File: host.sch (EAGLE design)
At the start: 109 parts, among them IC1 74LVC1T45GS,132, IC10 74LVC1T45GS,132, IC11 74LVC1T45GS,132, IC2 NCP187AMT120TAG, IC3 LD39200PU33R, IC4 74LVC1T45GS,132, IC5 74LVC1T45GS,132, IC6 74LVC1T45GS,132, IC7 74ALVC164245DGG:11, IC8 74ALVC164245DGG:11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

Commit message: Running through the checklist
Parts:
- added DONE: GREEN-0603, Seeed-LED:SMD-LED-CLEAR-GREEN(0603)
- added IC12: MMBT3904T, host:MMBT3904T
- added R29: 10K, rcl:R-EU_R0201
- added R30: 100K, rcl:R-EU_R0201
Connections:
- new net N$5: IC12.B, R30.2
- new net N$6: DONE.-, IC12.C
- new net N$7: DONE.+, R29.2
- net !STATUS!: now also U$1-RIGHT.GPIOL_71_!STATUS!@136
- net +3V3: now also R29.1
- net CDONE: now also R30.1
- net GND: now also IC12.E, IC7.1A7, IC7.1B7
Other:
- note added: "Checklist: [x] All power-pin checklist items [ ] Got as far as doing CDONE on configuration items"
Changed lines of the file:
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@@
 <setting verticaltext="up"/>
 </settings>
-<grid distance="0.1" unitdist="inch" unit="inch" style="lines" multiple="1" display="yes" altdistance="0.01" altunitdist="inch" altunit="inch"/>
+<grid distance="0.1" unitdist="inch" unit="inch" style="lines" multiple="1" display="no" altdistance="0.01" altunitdist="inch" altunit="inch"/>
 <layers>
 <layer number="1" name="Top" color="4" fill="1" visible="no" active="no"/>
@@
 <part name="SUPPLY28" library="supply2" deviceset="GND" device=""/>
 <part name="SUPPLY29" library="supply2" deviceset="GND" device=""/>
+<part name="DONE" library="Seeed-LED" deviceset="SMD-LED-CLEAR-GREEN(0603)" device="" value="GREEN-0603">
+<attribute name="USE" value="SML-E12M8WT86"/>
+</part>
+<part name="R29" library="rcl" library_urn="urn:adsk.eagle:library:334" deviceset="R-EU_" device="R0201" package3d_urn="urn:adsk.eagle:package:26117/2" value="10K">
+<attribute name="USE" value="WR02X221 JAL"/>
+</part>
+<part name="R30" library="rcl" library_urn="urn:adsk.eagle:library:334" deviceset="R-EU_" device="R0201" package3d_urn="urn:adsk.eagle:package:26117/2" value="100K">
+<attribute name="USE" value="PFR03S-104-JNH"/>
+</part>
+<part name="IC12" library="host" deviceset="MMBT3904T" device="">
+<attribute name="USE" value="MMBT3904T-7-F"/>
+</part>
+<part name="SUPPLY30" library="supply2" deviceset="GND" device=""/>
+<part name="+3V32" library="sjg-supply1" deviceset="+3V3" device=""/>
 </parts>
 <sheets>
 <sheet>
 <plain>
+<text x="12.7" y="243.84" size="1.778" layer="94">Checklist:
+[x]        All power-pin checklist items
+[ ]         Got as far as doing CDONE on configuration items</text>
 </plain>
 <instances>
@@
 <attribute name="VALUE" x="159.385" y="-125.095" size="1.778" layer="96"/>
 </instance>
+<instance part="DONE" gate="G$1" x="452.12" y="-20.32" smashed="yes" rot="R270">
+<attribute name="NAME" x="453.39" y="-12.7" size="1.27" layer="95" ratio="10" rot="R270"/>
+<attribute name="VALUE" x="447.04" y="-15.24" size="1.27" layer="96" ratio="10" rot="R270"/>
+<attribute name="USE" x="452.12" y="-20.32" size="1.778" layer="96" rot="R270" display="off"/>
+</instance>
+<instance part="R29" gate="G$1" x="452.12" y="-2.54" smashed="yes" rot="R270">
+<attribute name="NAME" x="453.6186" y="1.27" size="1.778" layer="95" rot="R270"/>
+<attribute name="VALUE" x="448.818" y="1.27" size="1.778" layer="96" rot="R270"/>
+<attribute name="USE" x="452.12" y="-2.54" size="1.778" layer="96" rot="R270" display="off"/>
+</instance>
+<instance part="R30" gate="G$1" x="421.64" y="-45.72" smashed="yes">
+<attribute name="NAME" x="417.83" y="-44.2214" size="1.778" layer="95"/>
+<attribute name="VALUE" x="417.83" y="-49.022" size="1.778" layer="96"/>
+<attribute name="USE" x="421.64" y="-45.72" size="1.778" layer="96" display="off"/>
+</instance>
+<instance part="IC12" gate="G$1" x="447.04" y="-45.72" smashed="yes">
+<attribute name="NAME" x="454.66" y="-38.1" size="1.778" layer="95"/>
+<attribute name="VALUE" x="454.66" y="-55.88" size="1.778" layer="96"/>
+<attribute name="USE" x="447.04" y="-45.72" size="1.778" layer="96" display="off"/>
+</instance>
+<instance part="SUPPLY30" gate="GND" x="452.12" y="-68.58" smashed="yes">
+<attribute name="VALUE" x="450.215" y="-71.755" size="1.778" layer="96"/>
+</instance>
+<instance part="+3V32" gate="G$1" x="452.12" y="12.7" smashed="yes" rot="MR0">
+<attribute name="VALUE" x="449.58" y="15.24" size="1.778" layer="96" rot="MR180"/>
+</instance>
 </instances>
 <busses>
@@
 <wire x1="124.46" y1="-53.34" x2="157.48" y2="-53.34" width="0.1524" layer="91"/>
 <label x="127" y="-53.34" size="1.778" layer="95"/>
-<label x="127" y="-55.88" size="1.778" layer="95"/>
 </segment>
 </net>
@@
 <wire x1="121.92" y1="-99.06" x2="124.46" y2="-101.6" width="0.1524" layer="91"/>
 <wire x1="124.46" y1="-101.6" x2="157.48" y2="-101.6" width="0.1524" layer="91"/>
+<label x="127" y="-101.6" size="1.778" layer="95"/>
 </segment>
 </net>
@@
 <wire x1="121.92" y1="-101.6" x2="124.46" y2="-104.14" width="0.1524" layer="91"/>
 <wire x1="124.46" y1="-104.14" x2="157.48" y2="-104.14" width="0.1524" layer="91"/>
+<label x="127" y="-104.14" size="1.778" layer="95"/>
 </segment>
 </net>
@@
 <wire x1="121.92" y1="-104.14" x2="124.46" y2="-106.68" width="0.1524" layer="91"/>
 <wire x1="124.46" y1="-106.68" x2="157.48" y2="-106.68" width="0.1524" layer="91"/>
+<label x="127" y="-106.68" size="1.778" layer="95"/>
 </segment>
 </net>
@@
 <wire x1="121.92" y1="-106.68" x2="124.46" y2="-109.22" width="0.1524" layer="91"/>
 <wire x1="124.46" y1="-109.22" x2="157.48" y2="-109.22" width="0.1524" layer="91"/>
+<label x="127" y="-109.22" size="1.778" layer="95"/>
 </segment>
 </net>
@@
 <wire x1="121.92" y1="-86.36" x2="124.46" y2="-88.9" width="0.1524" layer="91"/>
 <wire x1="124.46" y1="-88.9" x2="157.48" y2="-88.9" width="0.1524" layer="91"/>
+<label x="127" y="-88.9" size="1.778" layer="95"/>
 </segment>
 </net>
@@
 <wire x1="121.92" y1="-88.9" x2="124.46" y2="-91.44" width="0.1524" layer="91"/>
 <wire x1="124.46" y1="-91.44" x2="157.48" y2="-91.44" width="0.1524" layer="91"/>
+<label x="127" y="-91.44" size="1.778" layer="95"/>
 </segment>
 </net>
@@
 <wire x1="121.92" y1="-91.44" x2="124.46" y2="-93.98" width="0.1524" layer="91"/>
 <wire x1="124.46" y1="-93.98" x2="157.48" y2="-93.98" width="0.1524" layer="91"/>
+<label x="127" y="-93.98" size="1.778" layer="95"/>
 </segment>
 </net>
@@
 <wire x1="121.92" y1="-96.52" x2="124.46" y2="-99.06" width="0.1524" layer="91"/>
 <wire x1="124.46" y1="-99.06" x2="157.48" y2="-99.06" width="0.1524" layer="91"/>
+<label x="127" y="-99.06" size="1.778" layer="95"/>
 </segment>
 </net>
@@
 <wire x1="121.92" y1="-93.98" x2="124.46" y2="-96.52" width="0.1524" layer="91"/>
 <wire x1="124.46" y1="-96.52" x2="157.48" y2="-96.52" width="0.1524" layer="91"/>
+<label x="127" y="-96.52" size="1.778" layer="95"/>
 </segment>
 </net>
@@
 <wire x1="121.92" y1="-83.82" x2="124.46" y2="-86.36" width="0.1524" layer="91"/>
 <wire x1="124.46" y1="-86.36" x2="157.48" y2="-86.36" width="0.1524" layer="91"/>
+<label x="127" y="-86.36" size="1.778" layer="95"/>
 </segment>
 </net>
@@
 <wire x1="124.46" y1="-111.76" x2="157.48" y2="-111.76" width="0.1524" layer="91"/>
 <pinref part="DBG_CART" gate="A" pin="29"/>
+<label x="127" y="-111.76" size="1.778" layer="95"/>
 </segment>
 </net>
@@
 <wire x1="121.92" y1="-81.28" x2="124.46" y2="-83.82" width="0.1524" layer="91"/>
 <wire x1="124.46" y1="-83.82" x2="157.48" y2="-83.82" width="0.1524" layer="91"/>
+<label x="127" y="-83.82" size="1.778" layer="95"/>
 </segment>
 </net>
@@
 <wire x1="121.92" y1="-53.34" x2="124.46" y2="-55.88" width="0.1524" layer="91"/>
 <wire x1="124.46" y1="-55.88" x2="157.48" y2="-55.88" width="0.1524" layer="91"/>
+<label x="127" y="-55.88" size="1.778" layer="95"/>
 </segment>
 </net>
@@
 <pinref part="IC7" gate="G$1" pin="!1OE"/>
 <wire x1="180.34" y1="172.72" x2="185.42" y2="172.72" width="0.1524" layer="91"/>
-<wire x1="185.42" y1="172.72" x2="185.42" y2="167.64" width="0.1524" layer="91"/>
+<wire x1="185.42" y1="172.72" x2="185.42" y2="170.18" width="0.1524" layer="91"/>
 <junction x="185.42" y="167.64"/>
 <pinref part="IC7" gate="G$1" pin="!2OE"/>
+<wire x1="185.42" y1="170.18" x2="185.42" y2="167.64" width="0.1524" layer="91"/>
 <wire x1="180.34" y1="175.26" x2="185.42" y2="175.26" width="0.1524" layer="91"/>
 <wire x1="185.42" y1="175.26" x2="185.42" y2="172.72" width="0.1524" layer="91"/>
 <junction x="185.42" y="172.72"/>
+<pinref part="IC7" gate="G$1" pin="1B7"/>
+<wire x1="147.32" y1="208.28" x2="165.1" y2="208.28" width="0.1524" layer="91"/>
+<wire x1="165.1" y1="208.28" x2="165.1" y2="170.18" width="0.1524" layer="91"/>
+<wire x1="165.1" y1="170.18" x2="185.42" y2="170.18" width="0.1524" layer="91"/>
+<junction x="185.42" y="170.18"/>
+<pinref part="IC7" gate="G$1" pin="1A7"/>
+<wire x1="180.34" y1="208.28" x2="165.1" y2="208.28" width="0.1524" layer="91"/>
+<junction x="165.1" y="208.28"/>
 </segment>
 <segment>
@@
 <wire x1="161.29" y1="-109.22" x2="161.29" y2="-119.38" width="0.1524" layer="91"/>
 </segment>
+<segment>
+<pinref part="IC12" gate="G$1" pin="E"/>
+<pinref part="SUPPLY30" gate="GND" pin="GND"/>
+<wire x1="452.12" y1="-58.42" x2="452.12" y2="-66.04" width="0.1524" layer="91"/>
+</segment>
 </net>
 <net name="+3V3" class="0">
@@
 <wire x1="454.66" y1="60.96" x2="454.66" y2="63.5" width="0.1524" layer="91"/>
 </segment>
+<segment>
+<pinref part="R29" gate="G$1" pin="1"/>
+<wire x1="452.12" y1="2.54" x2="452.12" y2="10.16" width="0.1524" layer="91"/>
+<pinref part="+3V32" gate="G$1" pin="+3V3"/>
+</segment>
 </net>
 <net name="DIR_RW" class="0">
@@
 </segment>
 </net>
+<net name="!STATUS!" class="0">
+<segment>
+<pinref part="U$1" gate="-RIGHT" pin="GPIOL_71_!STATUS!@136"/>
+<wire x1="259.08" y1="144.78" x2="251.46" y2="144.78" width="0.1524" layer="91"/>
+<label x="250.952" y="145.288" size="1.778" layer="95" rot="R180"/>
+</segment>
+</net>
+<net name="N$5" class="0">
+<segment>
+<pinref part="R30" gate="G$1" pin="2"/>
+<pinref part="IC12" gate="G$1" pin="B"/>
+<wire x1="426.72" y1="-45.72" x2="434.34" y2="-45.72" width="0.1524" layer="91"/>
+</segment>
+</net>
+<net name="N$6" class="0">
+<segment>
+<pinref part="DONE" gate="G$1" pin="-"/>
+<pinref part="IC12" gate="G$1" pin="C"/>
+<wire x1="452.12" y1="-24.13" x2="452.12" y2="-33.02" width="0.1524" layer="91"/>
+</segment>
+</net>
+<net name="N$7" class="0">
+<segment>
+<pinref part="R29" gate="G$1" pin="2"/>
+<pinref part="DONE" gate="G$1" pin="+"/>
+<wire x1="452.12" y1="-7.62" x2="452.12" y2="-16.51" width="0.1524" layer="91"/>
+</segment>
+</net>
+<net name="CDONE" class="0">
+<segment>
+<pinref part="R30" gate="G$1" pin="1"/>
+<wire x1="416.56" y1="-45.72" x2="408.94" y2="-45.72" width="0.1524" layer="91"/>
+<label x="408.432" y="-45.212" size="1.778" layer="95" rot="R180"/>
+</segment>
+</net>

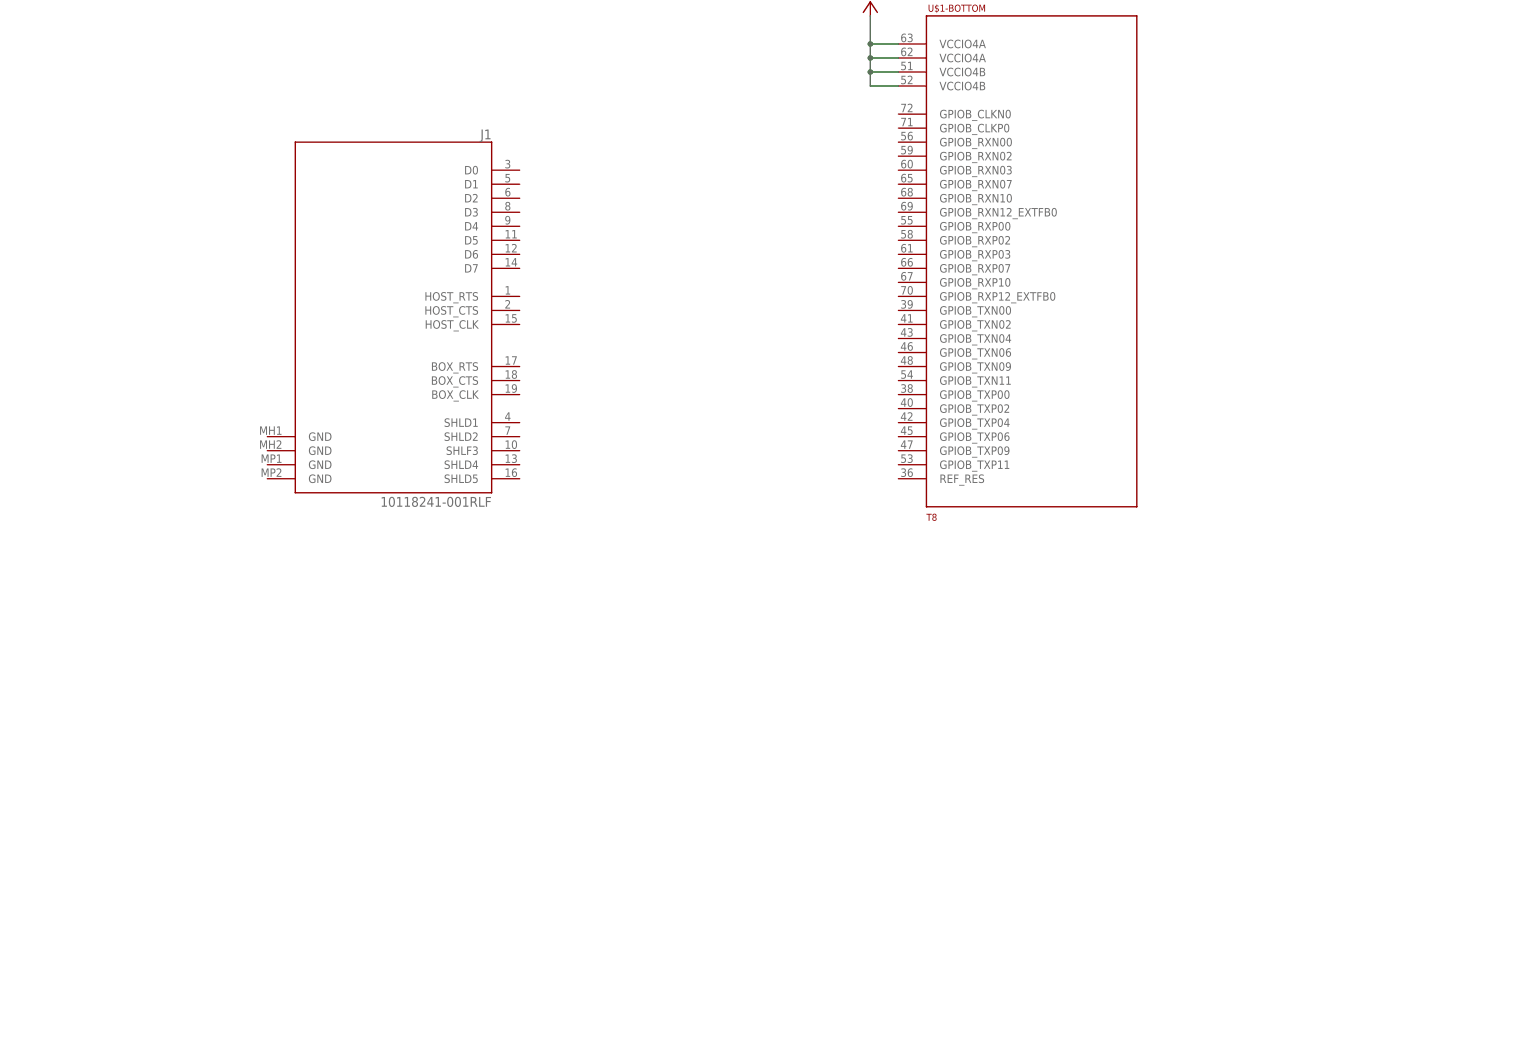
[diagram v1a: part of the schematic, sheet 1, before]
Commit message: Add the micro-HDMI interface
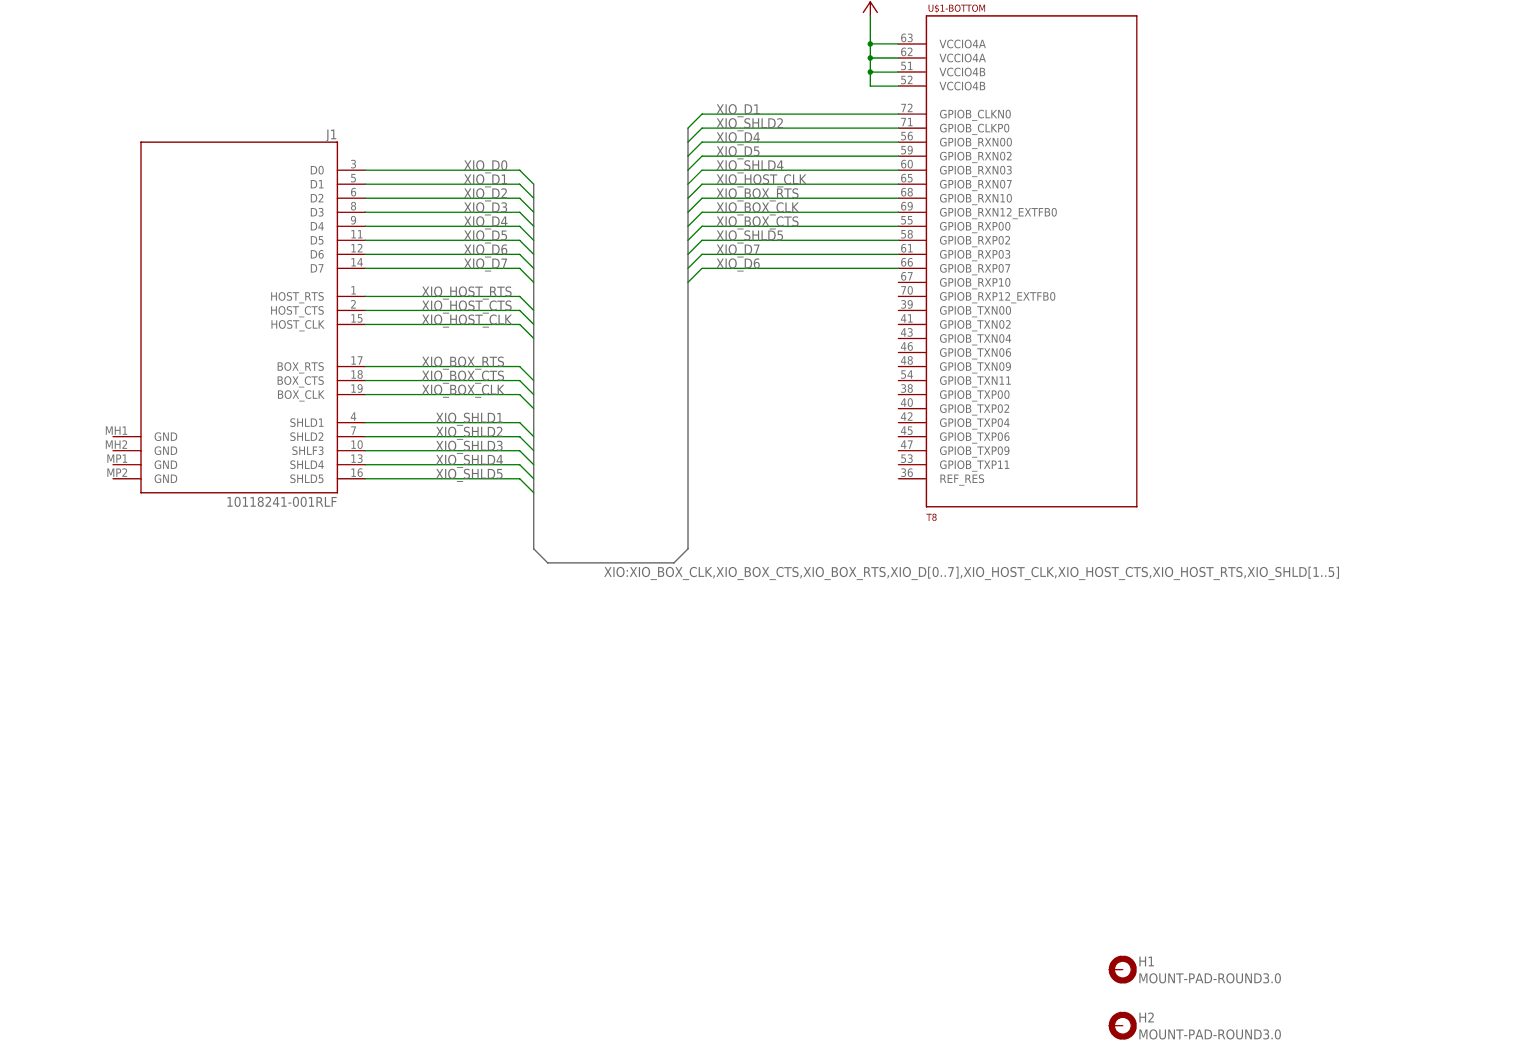
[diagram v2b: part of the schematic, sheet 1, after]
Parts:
- added H1, H2: MOUNT-PAD-ROUND3.0, holes:MOUNT-PAD-ROUND3.0
- added R31: 10K, rcl:R-EU_R0201
- added STATUS: GREEN-0603, Seeed-LED:SMD-LED-CLEAR-GREEN(0603)
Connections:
- new net N$9: R31.2, STATUS.+
- new net XIO_BOX_CLK: J1.BOX_CLK@19, U$1-BOTTOM.GPIOB_RXN12_EXTFB0@69
- new net XIO_BOX_CTS: J1.BOX_CTS@18, U$1-BOTTOM.GPIOB_RXP00@55
- new net XIO_BOX_RTS: J1.BOX_RTS@17, U$1-BOTTOM.GPIOB_RXN10@68
- new net XIO_D0: J1.D0@3, U$1-TOP.GPIOR_155@76
- new net XIO_D1: J1.D1@5, U$1-BOTTOM.GPIOB_CLKN0@72
- new net XIO_D2: J1.D2@6, U$1-TOP.GPIOR_136_CDI16@83
- new net XIO_D3: J1.D3@8, U$1-TOP.GPIOR_135_CDI17@84
- new net XIO_D4: J1.D4@9, U$1-BOTTOM.GPIOB_RXN00@56
- new net XIO_D5: J1.D5@11, U$1-BOTTOM.GPIOB_RXN02@59
- new net XIO_D6: J1.D6@12, U$1-BOTTOM.GPIOB_RXP07@66
- new net XIO_D7: J1.D7@14, U$1-BOTTOM.GPIOB_RXP03@61
- new net XIO_HOST_CLK: J1.HOST_CLK@15, U$1-BOTTOM.GPIOB_RXN07@65
- new net XIO_HOST_CTS: J1.HOST_CTS@2, U$1-TOP.GPIOR_139@81
- new net XIO_HOST_RTS: J1.HOST_RTS@1, U$1-TOP.GPIOR_154@77
- new net XIO_SHLD1: J1.SHLD1@4, U$1-TOP.GPIOR_138@82
- new net XIO_SHLD2: J1.SHLD2@7, U$1-BOTTOM.GPIOB_CLKP0@71
- new net XIO_SHLD3: J1.SHLF3@10, U$1-TOP.GPIOR_133_CDI18@86
- new net XIO_SHLD4: J1.SHLD4@13, U$1-BOTTOM.GPIOB_RXN03@60
- new net XIO_SHLD5: J1.SHLD5@16, U$1-BOTTOM.GPIOB_RXP02@58
- net !STATUS!: now also STATUS.-
- net +3V3: now also R31.1
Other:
- moved on the sheet: J1

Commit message: Autorouted
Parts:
- added C54: 100nF, rcl:C-EUC0201
- added DBG_XIO0, DBG_XIO1: (no value), pinhead:PINHD-2X5
- added LD0, LD1, LD2: GREEN-0603, Seeed-LED:SMD-LED-CLEAR-GREEN(0603)
- added R32: 12K, rcl:R-EU_R0201
- added R33, R34, R35: 220R, rcl:R-EU_R0201
- IC1, IC10, IC11, IC4, IC5, IC6, IC9: USE (none) -> 74LVC1T45GS,132
- R29, R31: value 10K -> 220R
- renumbered J1 to UHDMI, JP1 to TTAG
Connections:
- new net LED0: LD0.-, U$1-BOTTOM.GPIOB_TXN00@39
- new net LED1: LD1.-, U$1-BOTTOM.GPIOB_TXN02@41
- new net LED2: LD2.-, U$1-BOTTOM.GPIOB_TXN04@43
- new net N$13: LD0.+, R33.2
- new net N$15: LD1.+, R34.2
- new net N$16: LD2.+, R35.2
- new net N$8: R32.2, U$1-BOTTOM.REF_RES@36
- net +3V3: now also C54.1, R33.1, R34.1, R35.1
- net GND: now also C54.2, DBG_XIO1.10, H1.MOUNT, H2.MOUNT, R32.1
- net XIO_BOX_CLK: now also DBG_XIO0.9
- net XIO_BOX_CTS: now also DBG_XIO1.9
- net XIO_BOX_RTS: now also DBG_XIO1.1
- net XIO_D0: now also DBG_XIO0.1, U$1-TOP.GPIOR_135_CDI17@84; no longer U$1-TOP.GPIOR_155@76
- net XIO_D1: now also DBG_XIO0.7
- net XIO_D2: now also DBG_XIO0.6, U$1-TOP.GPIOR_139@81; no longer U$1-TOP.GPIOR_136_CDI16@83
- net XIO_D3: now also DBG_XIO0.5, U$1-TOP.GPIOR_154@77; no longer U$1-TOP.GPIOR_135_CDI17@84
- net XIO_D4: now also DBG_XIO1.8
- net XIO_D5: now also DBG_XIO1.6
- net XIO_D6: now also DBG_XIO1.2
- net XIO_D7: now also DBG_XIO1.4
- net XIO_HOST_CLK: now also DBG_XIO1.3
- net XIO_HOST_CTS: now also DBG_XIO0.4, U$1-TOP.GPIOR_136_CDI16@83; no longer U$1-TOP.GPIOR_139@81
- net XIO_HOST_RTS: now also DBG_XIO0.2, U$1-TOP.GPIOR_133_CDI18@86; no longer U$1-TOP.GPIOR_154@77
- net XIO_SHLD1: now also DBG_XIO0.3
- net XIO_SHLD2: now also DBG_XIO0.10
- net XIO_SHLD3: now also DBG_XIO0.8, U$1-TOP.GPIOR_155@76; no longer U$1-TOP.GPIOR_133_CDI18@86
- net XIO_SHLD4: now also DBG_XIO1.5
- net XIO_SHLD5: now also DBG_XIO1.7
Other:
- note added: "Checklist: [x] All T8 checklist items [x] Directionality of level xlators"
- note removed: "Checklist: [x] All power-pin checklist items [ ] Got as far as doing CDONE on configuration items"
- moved on the sheet: H1, H2, U$1-TOP
